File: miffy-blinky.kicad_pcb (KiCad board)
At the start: 2 copper layers, 65.3 x 91.9 mm, 18 parts, among them J1 Conn_01x02_Socket, U1 NE555P, U2 4017

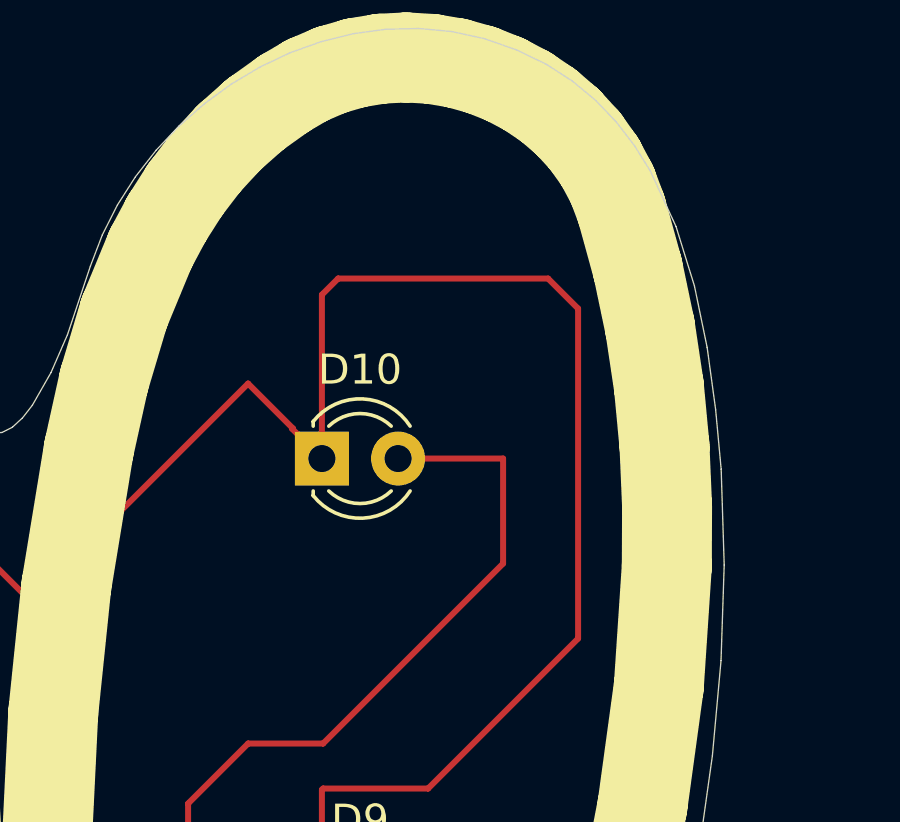
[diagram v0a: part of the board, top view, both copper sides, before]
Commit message: added keychain hole and updated gerbers
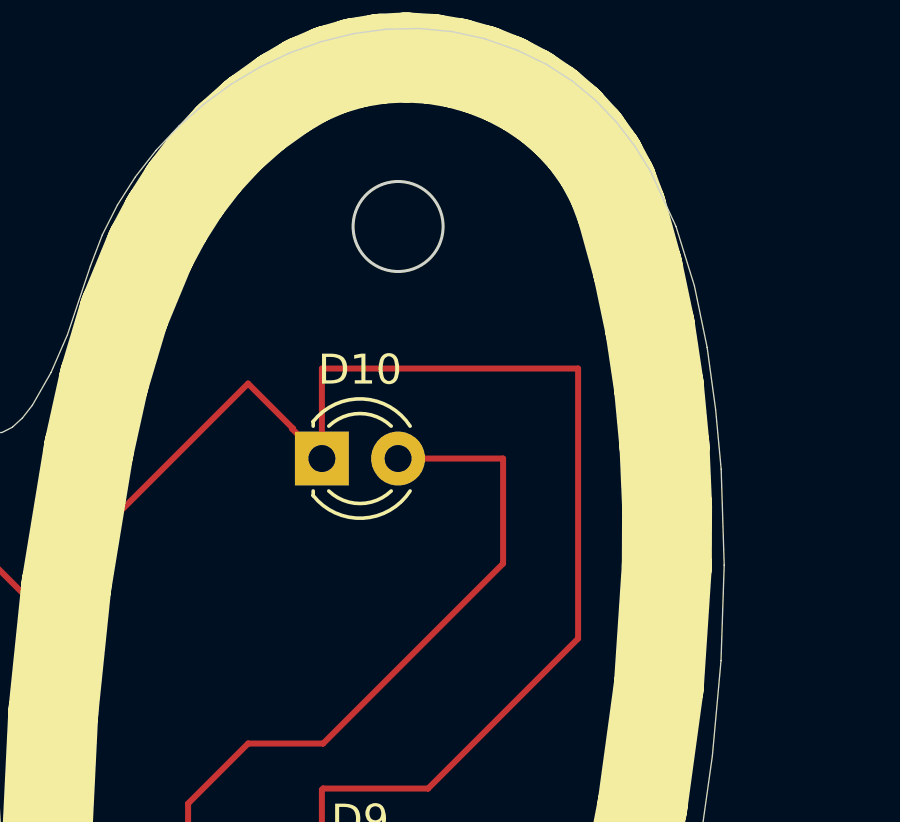
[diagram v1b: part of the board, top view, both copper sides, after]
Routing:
- net Net-(D1-K): track 308.5 -> 303.4 mm
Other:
- outline, holes or cut-outs redrawn
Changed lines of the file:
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@@
 			(outputformat 1)
 			(mirror no)
-			(drillshape 1)
+			(drillshape 0)
 			(scaleselection 1)
-			(outputdirectory "")
+			(outputdirectory "gerbers/")
 		)
 	)
@@
 		(layer "Edge.Cuts")
 	)
+	(gr_circle
+		(center 220 56.265279)
+		(end 221.5 56.265279)
+		(stroke
+			(width 0.1)
+			(type solid)
+		)
+		(fill no)
+		(layer "Edge.Cuts")
+	)
 	(gr_line
 		(start 220.688878 49.664296)
@@
 	)
 	(segment
+		(start 217.46 61)
+		(end 226 61)
+		(width 0.2)
+		(layer "F.Cu")
+		(net "Net-(D1-K)")
+	)
+	(segment
 		(start 214.69 107.5)
 		(end 214.69 109.69)
@@
 	)
 	(segment
-		(start 225 58)
-		(end 226 59)
-		(width 0.2)
-		(layer "F.Cu")
-		(net "Net-(D1-K)")
-	)
-	(segment
 		(start 193.96 133.46)
 		(end 193.96 131.5)
@@
 	)
 	(segment
-		(start 221 75)
-		(end 217.5 75)
+		(start 226 61)
+		(end 226 70)
 		(width 0.2)
 		(layer "F.Cu")
@@
 	)
 	(segment
-		(start 226 70)
-		(end 221 75)
-		(width 0.2)
-		(layer "F.Cu")
-		(net "Net-(D1-K)")
-	)
-	(segment
-		(start 217.46 64)
-		(end 217.46 58.54)
-		(width 0.2)
-		(layer "F.Cu")
-		(net "Net-(D1-K)")
-	)
-	(segment
 		(start 214.69 109.69)
 		(end 215.5 110.5)
@@
 	)
 	(segment
-		(start 218 58)
-		(end 225 58)
-		(width 0.2)
-		(layer "F.Cu")
-		(net "Net-(D1-K)")
-	)
-	(segment
 		(start 230 97)
 		(end 230 108)
@@
 	)
 	(segment
-		(start 217.5 75)
-		(end 217.46 75.04)
-		(width 0.2)
-		(layer "F.Cu")
-		(net "Net-(D1-K)")
-	)
-	(segment
 		(start 215 61.5)
 		(end 216.5 63)
@@
 	)
 	(segment
+		(start 217.5 75)
+		(end 217.46 75.04)
+		(width 0.2)
+		(layer "F.Cu")
+		(net "Net-(D1-K)")
+	)
+	(segment
 		(start 216 108.81)
 		(end 214.69 107.5)
@@
 	)
 	(segment
+		(start 217.46 75.04)
+		(end 217.46 79)
+		(width 0.2)
+		(layer "F.Cu")
+		(net "Net-(D1-K)")
+	)
+	(segment
 		(start 219.5 76.5)
 		(end 223.5 76.5)
@@
 	)
 	(segment
-		(start 217.46 58.54)
-		(end 218 58)
+		(start 217.46 64)
+		(end 217.46 61)
 		(width 0.2)
 		(layer "F.Cu")
@@
 	)
 	(segment
-		(start 217.46 75.04)
-		(end 217.46 79)
+		(start 216 109.5)
+		(end 216 108.81)
 		(width 0.2)
 		(layer "F.Cu")
@@
 	)
 	(segment
-		(start 216 109.5)
-		(end 216 108.81)
+		(start 226 70)
+		(end 221 75)
 		(width 0.2)
 		(layer "F.Cu")
@@
 	)
 	(segment
+		(start 221 75)
+		(end 217.5 75)
+		(width 0.2)
+		(layer "F.Cu")
+		(net "Net-(D1-K)")
+	)
+	(segment
 		(start 230 108)
 		(end 228.5 109.5)
@@
 		(width 0.2)
 		(layer "F.Cu")
-		(net "Net-(D1-K)")
-	)
-	(segment
-		(start 226 59)
-		(end 226 70)
-		(width 0.2)
-		(layer "F.Cu")
